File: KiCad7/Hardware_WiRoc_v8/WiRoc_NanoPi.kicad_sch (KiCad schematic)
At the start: 56 parts, among them J1 Conn_02x05_Odd_Even, J10 Conn_01x09_Socket, J2 Conn_01x04, J5 Conn_01x04_Socket, J6 HAT_Conn_DBG, J8 Conn_01x06, J9 Conn_Coaxial, SW1 SW_SPST, U1 DRF1268DS, U2 OLED, U3 AXP209, U5 SY6280, U6 BatteryPadM, U7 BatteryPadP

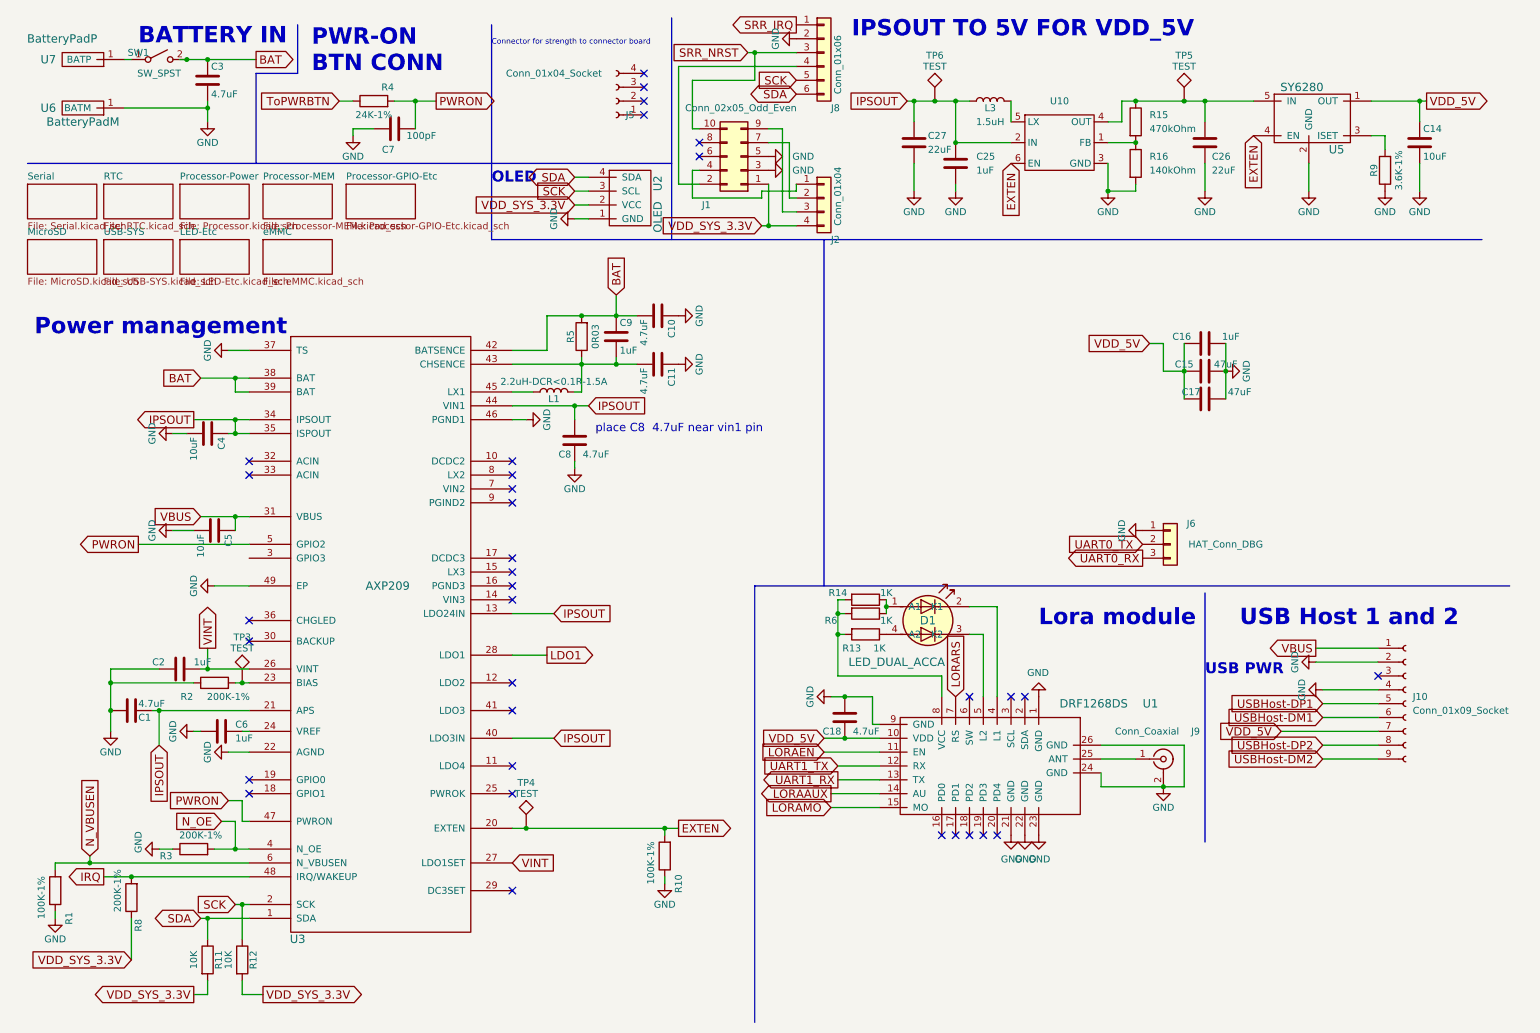
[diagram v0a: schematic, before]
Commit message: wiroc v8 layout work
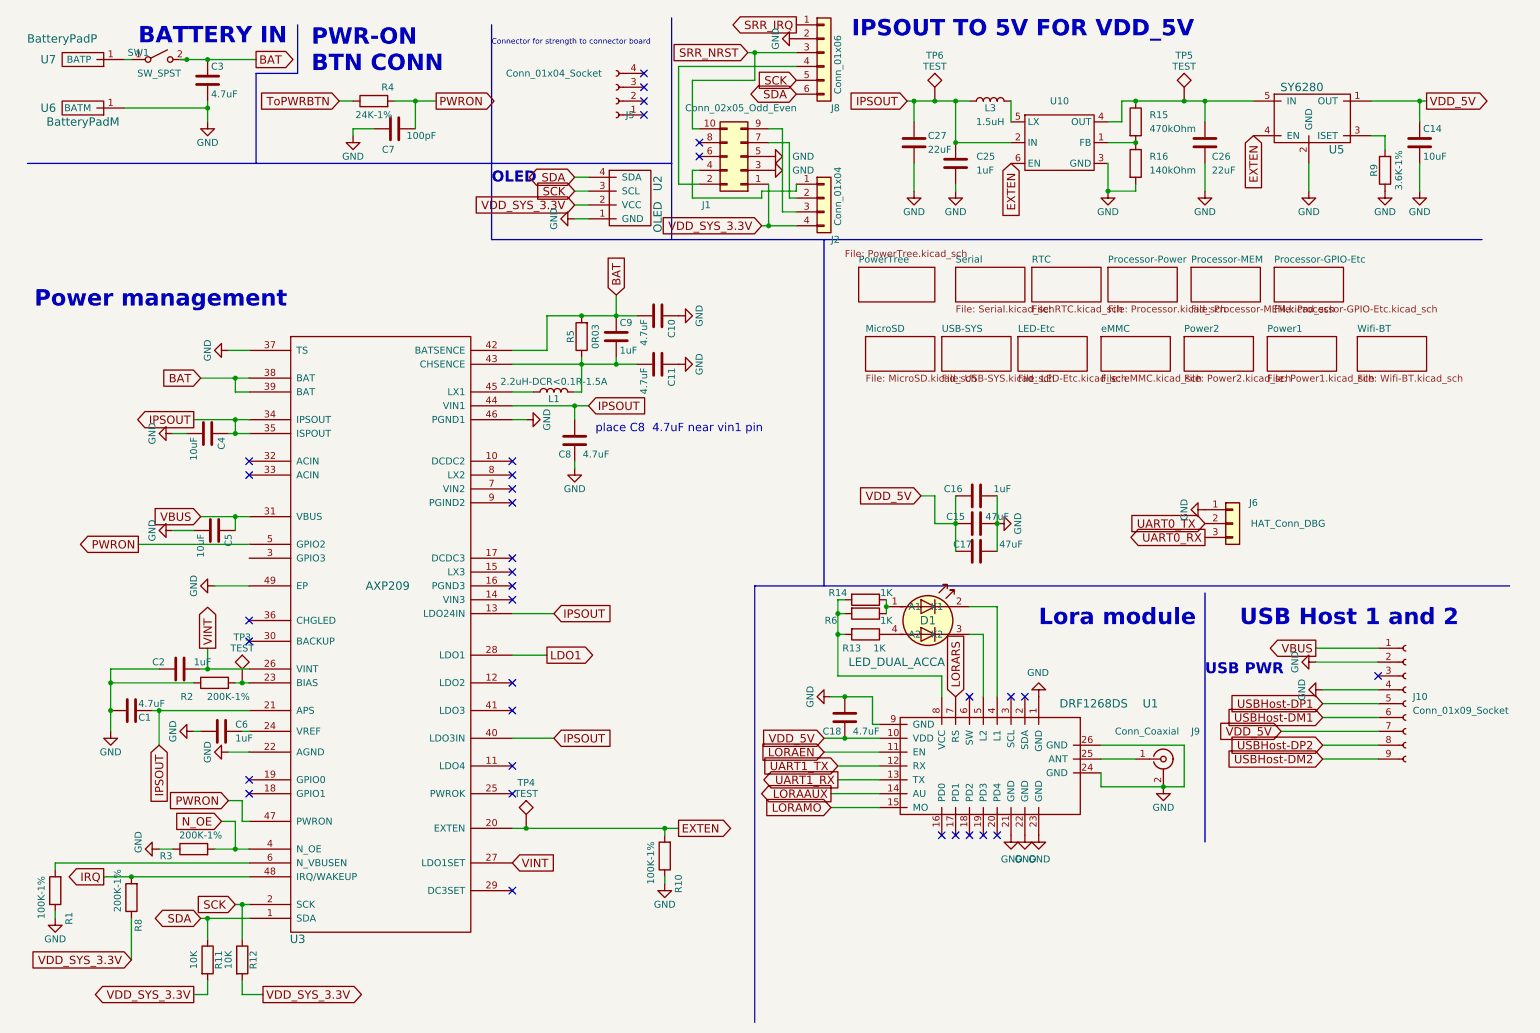
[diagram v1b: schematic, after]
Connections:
- net N_VBUSEN: no longer names the net of R1.2, U3.6 (N_VBUSEN)
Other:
- added sheet Power1 (Power1.kicad_sch)
- added sheet Power2 (Power2.kicad_sch)
- added sheet PowerTree (PowerTree.kicad_sch)
- added sheet Wifi-BT (Wifi-BT.kicad_sch)
- moved on the sheet: C15, C16, C17, J6
